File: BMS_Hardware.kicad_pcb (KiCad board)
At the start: 2 copper layers, 16.4 x 2.4 mm, 27 parts, among them Q1 2N7002PW, Q2 2N7002PW, Q3 2N7002PW, Q4 2N7002PW, Q5 2N7002PW, Q8 2N7002PW, Q9 2N7002PW, U1 ACS759ECB-200B-PFF-T, U10 E_STOP+LED, U11 TEMP_1, U12 FAN_4, U17 Indicator Comm, U18 OKI, U2 FAN_1, U21 TM4C129E_Launchpad, U4 FAN_2, U5 LOGIC_SWITCH, U6 LT1910, U7 E_STOP, U8 FAN_3

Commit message: started board edgecuts
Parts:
- added C1: 1u, Capacitor_SMD:C_0603_1608Metric_Pad1.05x0.95mm_HandSolder, F.Cu at (350.1, 110.8)
- added C10: 10u, Capacitor_SMD:C_0603_1608Metric_Pad1.05x0.95mm_HandSolder, F.Cu at (346.4, 112.8)
- added C11: 1u, Capacitor_SMD:C_0603_1608Metric_Pad1.05x0.95mm_HandSolder, F.Cu at (350.1, 107.7)
- added C12: 1u, Capacitor_SMD:C_0603_1608Metric_Pad1.05x0.95mm_HandSolder, F.Cu at (357.1, 100.9)
- added C13: 1u, Capacitor_SMD:C_0603_1608Metric_Pad1.05x0.95mm_HandSolder, F.Cu at (329.3, 130.2)
- added C14: 1u, Capacitor_SMD:C_0603_1608Metric_Pad1.05x0.95mm_HandSolder, F.Cu at (343.1, 115.9)
- added C15: 1u, Capacitor_SMD:C_0603_1608Metric_Pad1.05x0.95mm_HandSolder, F.Cu at (314.0, 114.6)
- added C16: 1u, Capacitor_SMD:C_0603_1608Metric_Pad1.05x0.95mm_HandSolder, F.Cu at (343.1, 114.4)
- added C17: 22u 50V, Capacitor_THT:CP_Radial_D6.3mm_P2.50mm, F.Cu at (350.8, 102.0)
- added C18: 10u, Capacitor_SMD:C_0603_1608Metric_Pad1.05x0.95mm_HandSolder, F.Cu at (336.0, 130.9)
- added C19: 10u, Capacitor_SMD:C_0603_1608Metric_Pad1.05x0.95mm_HandSolder, F.Cu at (353.5, 112.3)
- added C2: 1u, Capacitor_SMD:C_0603_1608Metric_Pad1.05x0.95mm_HandSolder, F.Cu at (343.1, 117.4)
- added C20: 10u, Capacitor_SMD:C_0603_1608Metric_Pad1.05x0.95mm_HandSolder, F.Cu at (343.7, 121.9)
- added C23: 10u, Capacitor_SMD:C_0603_1608Metric_Pad1.05x0.95mm_HandSolder, F.Cu at (347.0, 118.8)
- added C24: 0.1u, Capacitor_SMD:C_0603_1608Metric_Pad1.05x0.95mm_HandSolder, F.Cu at (339.6, 127.2)
- added C26: 22u 50V, Capacitor_THT:CP_Radial_D6.3mm_P2.50mm, F.Cu at (330.6, 122.2)
- added C27: 10u, Capacitor_SMD:C_0603_1608Metric_Pad1.05x0.95mm_HandSolder, F.Cu at (349.8, 116.8)
- added C28: 10u, Capacitor_SMD:C_0603_1608Metric_Pad1.05x0.95mm_HandSolder, F.Cu at (336.9, 121.1)
- added C29: 10u, Capacitor_SMD:C_0603_1608Metric_Pad1.05x0.95mm_HandSolder, F.Cu at (332.9, 126.4)
- added C3: 1u, Capacitor_SMD:C_0603_1608Metric_Pad1.05x0.95mm_HandSolder, F.Cu at (346.4, 114.3)
- added C30: 10u, Capacitor_SMD:C_0603_1608Metric_Pad1.05x0.95mm_HandSolder, F.Cu at (332.6, 129.6)
- added C31: 0.1u, Capacitor_SMD:C_0603_1608Metric_Pad1.05x0.95mm_HandSolder, F.Cu at (350.1, 112.3)
- added C4: 1u, Capacitor_SMD:C_0603_1608Metric_Pad1.05x0.95mm_HandSolder, F.Cu at (332.9, 127.9)
- added C5: 1u, Capacitor_SMD:C_0603_1608Metric_Pad1.05x0.95mm_HandSolder, F.Cu at (340.3, 119.2)
- added C6: 1u, Capacitor_SMD:C_0603_1608Metric_Pad1.05x0.95mm_HandSolder, F.Cu at (336.9, 122.7)
- added C7: 1u, Capacitor_SMD:C_0603_1608Metric_Pad1.05x0.95mm_HandSolder, F.Cu at (357.1, 102.4)
- added C8: 1u, Capacitor_SMD:C_0603_1608Metric_Pad1.05x0.95mm_HandSolder, F.Cu at (350.1, 109.3)
- added C9: 1u, Capacitor_SMD:C_0603_1608Metric_Pad1.05x0.95mm_HandSolder, F.Cu at (353.5, 106.2)
- added D1: 7.5V, Diode_SMD:D_SOD-323_HandSoldering, F.Cu at (308.0, 127.7)
- added D10: V_OUT_LED, LED_SMD:LED_0603_1608Metric_Pad1.05x0.95mm_HandSolder, F.Cu at (343.1, 112.8)
- added D11: 3.6V, Diode_SMD:D_SOD-323_HandSoldering, F.Cu at (402.5, 175.1)
- added D12: D_Schottky, Diode_SMD:D_0603_1608Metric_Pad1.05x0.95mm_HandSolder, F.Cu at (350.2, 106.2)
- added D13: D_Schottky, Diode_SMD:D_0603_1608Metric_Pad1.05x0.95mm_HandSolder, F.Cu at (357.2, 99.3)
- added D14: D_Schottky, Diode_SMD:D_0603_1608Metric_Pad1.05x0.95mm_HandSolder, F.Cu at (329.5, 126.4)
- added D15: D_Schottky, Diode_SMD:D_0603_1608Metric_Pad1.05x0.95mm_HandSolder, F.Cu at (337.0, 119.6)
- added D16: D_Schottky, Diode_SMD:D_0603_1608Metric_Pad1.05x0.95mm_HandSolder, F.Cu at (339.7, 117.6)
- added D17: D_Schottky, Diode_SMD:D_0603_1608Metric_Pad1.05x0.95mm_HandSolder, F.Cu at (339.7, 114.4)
- added D18: D_Schottky, Diode_SMD:D_0603_1608Metric_Pad1.05x0.95mm_HandSolder, F.Cu at (315.7, 129.5)
- added D19: D_Schottky, Diode_SMD:D_0603_1608Metric_Pad1.05x0.95mm_HandSolder, F.Cu at (325.9, 130.2)
- added D2: 7.5V, Diode_SMD:D_SOD-323_HandSoldering, F.Cu at (312.0, 127.7)
- added D20: D_Schottky, Diode_SMD:D_0603_1608Metric_Pad1.05x0.95mm_HandSolder, F.Cu at (319.1, 130.2)
- added D21: D_Schottky, Diode_SMD:D_0603_1608Metric_Pad1.05x0.95mm_HandSolder, F.Cu at (322.5, 130.2)
- added D22: D_Schottky, Diode_SMD:D_0603_1608Metric_Pad1.05x0.95mm_HandSolder, F.Cu at (339.7, 116.0)
- added D23: D_Schottky, Diode_SMD:D_0603_1608Metric_Pad1.05x0.95mm_HandSolder, F.Cu at (329.5, 128.0)
- added D3: 7.5V, Diode_SMD:D_SOD-323_HandSoldering, F.Cu at (316.1, 127.7)
- added D4: 7.5V, Diode_SMD:D_SOD-323_HandSoldering, F.Cu at (312.0, 129.7)
- added D5: 7.5V, Diode_SMD:D_SOD-323_HandSoldering, F.Cu at (308.0, 129.7)
- added D6: 7.5V, Diode_SMD:D_SOD-323_HandSoldering, F.Cu at (402.5, 177.0)
- added D7: 7.5V, Diode_SMD:D_SOD-323_HandSoldering, F.Cu at (314.4, 112.8)
- added D8: 7.5V, Diode_SMD:D_SOD-323_HandSoldering, F.Cu at (314.4, 110.9)
- added D9: LOG_PWR_LED, LED_SMD:LED_0603_1608Metric_Pad1.05x0.95mm_HandSolder, F.Cu at (339.7, 112.8)
- added F1: PTC2920, Fuse:Fuse_2920_7451Metric, F.Cu at (323.2, 126.4)
- added Q6: IRLS3034-7P, MRDT_Actives:IRLS3034_TO-263-7_P, F.Cu at (310.2, 121.1)
- added Q7: IRLS3034-7P, MRDT_Actives:IRLS3034_TO-263-7_P, F.Cu at (320.7, 104.2)
- added R1: 10k, Resistor_SMD:R_0603_1608Metric_Pad1.05x0.95mm_HandSolder, F.Cu at (336.9, 124.2)
- added R10: 100K, Resistor_SMD:R_0603_1608Metric_Pad1.05x0.95mm_HandSolder, F.Cu at (343.7, 120.4)
- added R11: 10K, Resistor_SMD:R_0603_1608Metric_Pad1.05x0.95mm_HandSolder, F.Cu at (340.3, 123.7)
- added R12: 100K, Resistor_SMD:R_0603_1608Metric_Pad1.05x0.95mm_HandSolder, F.Cu at (356.9, 106.9)
- added R13: 10k, Resistor_SMD:R_0603_1608Metric_Pad1.05x0.95mm_HandSolder, F.Cu at (346.4, 117.3)
- added R14: 1M, Resistor_SMD:R_0603_1608Metric_Pad1.05x0.95mm_HandSolder, F.Cu at (349.8, 113.8)
- added R15: 100k, Resistor_SMD:R_0603_1608Metric_Pad1.05x0.95mm_HandSolder, F.Cu at (353.5, 110.8)
- added R16: 10k, Resistor_SMD:R_0603_1608Metric_Pad1.05x0.95mm_HandSolder, F.Cu at (336.0, 129.4)
- added R17: 36.5k, Resistor_SMD:R_0603_1608Metric_Pad1.05x0.95mm_HandSolder, F.Cu at (349.8, 115.3)
- added R18: 4k, Resistor_SMD:R_0603_1608Metric_Pad1.05x0.95mm_HandSolder, F.Cu at (356.8, 108.4)
- added R19: 10k, Resistor_SMD:R_0603_1608Metric_Pad1.05x0.95mm_HandSolder, F.Cu at (353.5, 109.3)
- added R2: 36.5k, Resistor_SMD:R_0603_1608Metric_Pad1.05x0.95mm_HandSolder, F.Cu at (357.1, 103.9)
- added R20: 100K, Resistor_SMD:R_0603_1608Metric_Pad1.05x0.95mm_HandSolder, F.Cu at (343.6, 123.5)
- added R21: 36.5k, Resistor_SMD:R_0603_1608Metric_Pad1.05x0.95mm_HandSolder, F.Cu at (353.1, 113.8)
- added R22: 1M, Resistor_SMD:R_0603_1608Metric_Pad1.05x0.95mm_HandSolder, F.Cu at (356.8, 110.0)
- added R23: 100k, Resistor_SMD:R_0603_1608Metric_Pad1.05x0.95mm_HandSolder, F.Cu at (340.3, 125.2)
- added R24: 100K, Resistor_SMD:R_0603_1608Metric_Pad1.05x0.95mm_HandSolder, F.Cu at (339.3, 128.7)
- added R25: 330, Resistor_SMD:R_0603_1608Metric_Pad1.05x0.95mm_HandSolder, F.Cu at (356.8, 111.5)
- added R26: 330, Resistor_SMD:R_0603_1608Metric_Pad1.05x0.95mm_HandSolder, F.Cu at (353.1, 115.3)
- added R27: 1M, Resistor_SMD:R_0603_1608Metric_Pad1.05x0.95mm_HandSolder, F.Cu at (343.6, 125.0)
- added R28: 100k, Resistor_SMD:R_0603_1608Metric_Pad1.05x0.95mm_HandSolder, F.Cu at (347.0, 121.9)
- added R29: 4.7k, Resistor_SMD:R_0603_1608Metric_Pad1.05x0.95mm_HandSolder, F.Cu at (350.4, 118.3)
- added R3: 10k, Resistor_SMD:R_0603_1608Metric_Pad1.05x0.95mm_HandSolder, F.Cu at (353.5, 107.7)
- added R30: 36.5k, Resistor_SMD:R_0603_1608Metric_Pad1.05x0.95mm_HandSolder, F.Cu at (342.9, 126.7)
- added R31: 36.5k, Resistor_SMD:R_0603_1608Metric_Pad1.05x0.95mm_HandSolder, F.Cu at (340.3, 120.7)
- added R32: 36.5k, Resistor_SMD:R_0603_1608Metric_Pad1.05x0.95mm_HandSolder, F.Cu at (353.1, 116.8)
- added R33: 36.5k, Resistor_SMD:R_0603_1608Metric_Pad1.05x0.95mm_HandSolder, F.Cu at (356.8, 113.0)
- added R34: 36.5k, Resistor_SMD:R_0603_1608Metric_Pad1.05x0.95mm_HandSolder, F.Cu at (336.2, 127.2)
- added R4: 10k, Resistor_SMD:R_0603_1608Metric_Pad1.05x0.95mm_HandSolder, F.Cu at (357.1, 105.4)
- added R5: 10k, Resistor_SMD:R_0603_1608Metric_Pad1.05x0.95mm_HandSolder, F.Cu at (336.9, 125.7)
- added R6: 10k, Resistor_SMD:R_0603_1608Metric_Pad1.05x0.95mm_HandSolder, F.Cu at (340.3, 122.2)
- added R7: 10k, Resistor_SMD:R_0603_1608Metric_Pad1.05x0.95mm_HandSolder, F.Cu at (347.0, 120.4)
- added R8: 10k, Resistor_SMD:R_0603_1608Metric_Pad1.05x0.95mm_HandSolder, F.Cu at (343.7, 118.9)
- added R9: 10k, Resistor_SMD:R_0603_1608Metric_Pad1.05x0.95mm_HandSolder, F.Cu at (346.4, 115.8)
- added U13: INA132, Package_SO:SO-8_5.3x6.2mm_P1.27mm, F.Cu at (333.9, 108.7)
- added U14: INA132, Package_SO:SO-8_5.3x6.2mm_P1.27mm, F.Cu at (391.3, 63.9)
- added U15: INA132, Package_SO:SO-8_5.3x6.2mm_P1.27mm, F.Cu at (323.4, 120.0)
- added U16: OKI, MRDT_Devices:OKI_Horizontal, F.Cu at (302.1, 98.8)
- added U19: INA132, Package_SO:SO-8_5.3x6.2mm_P1.27mm, F.Cu at (333.1, 115.4)
- added U20: INA132, Package_SO:SO-8_5.3x6.2mm_P1.27mm, F.Cu at (343.6, 108.7)
- added U3: INA132, Package_SO:SO-8_5.3x6.2mm_P1.27mm, F.Cu at (333.9, 101.9)
- added U9: INA132, Package_SO:SO-8_5.3x6.2mm_P1.27mm, F.Cu at (323.4, 113.3)
- moved Q5 209.7 mm to (310.4, 177.4)
- moved Conn2 209.7 mm to (340.8, 171.7)
- moved Q4 209.7 mm to (315.9, 177.4)
- moved U11 209.7 mm to (341.1, 176.0)
- moved U12 209.7 mm to (373.3, 171.5)
- moved U17 209.7 mm to (351.6, 176.0)
- moved U2 209.7 mm to (373.3, 178.0)
- moved U5 209.7 mm to (360.0, 171.7)
- moved U7 209.7 mm to (381.0, 171.5)
- moved U8 209.7 mm to (381.0, 178.0)
- moved C32 209.7 mm to (317.6, 171.5)
- moved Q3 209.7 mm to (321.3, 177.4)
- moved Q8 209.7 mm to (305.0, 177.4)
- moved Q9 209.7 mm to (299.5, 177.4)
- moved U10 209.7 mm to (334.4, 178.5)
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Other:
- board size 16.4 x 2.4 mm -> 208.3 x 76.2 mm

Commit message: work done on board layout
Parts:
- moved U8 348.4 mm to (48.0, 75.7)
- moved U2 346.4 mm to (48.0, 59.1)
- moved U12 336.9 mm to (48.0, 83.9)
- moved U4 336.5 mm to (48.0, 67.3)
- moved U7 336.1 mm to (64.6, 58.1)
- moved U5 307.8 mm to (66.8, 77.8)
- moved V1 307.5 mm to (61.7, 105.8)
- moved R12 305.0 mm to (54.9, 64.7)
- moved Q1 301.3 mm to (54.8, 59.7), turned to 270 degrees
- moved R10 296.1 mm to (54.8, 55.7)
- moved R20 292.9 mm to (55.0, 73.6)
- moved R18 289.5 mm to (71.4, 60.4)
- moved U10 289.3 mm to (67.0, 68.1)
- moved R24 288.1 mm to (55.0, 82.2)
- moved R19 283.0 mm to (75.5, 55.9)
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
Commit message: halfway done with alyout
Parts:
- moved C19 180.6 mm to (183.4, 104.3), turned to 90 degrees
- moved C17 179.5 mm to (171.8, 114.4), turned to 90 degrees
- moved C27 172.2 mm to (179.9, 88.4), turned to 270 degrees
- moved C26 160.5 mm to (171.9, 98.1), turned to 90 degrees
- moved C18 159.0 mm to (179.2, 104.2), turned to 90 degrees
- moved C20 157.1 mm to (187.6, 104.2), turned to 90 degrees
- moved C28 156.4 mm to (184.0, 88.4), turned to 270 degrees
- moved C23 156.0 mm to (191.7, 104.2), turned to 90 degrees
- moved C31 155.7 mm to (196.2, 88.5), turned to 270 degrees
- moved C29 149.7 mm to (188.1, 88.5), turned to 270 degrees
- moved C30 146.4 mm to (192.1, 88.5), turned to 270 degrees
- moved C24 145.6 mm to (195.8, 104.2), turned to 90 degrees
- moved U18 142.9 mm to (179.1, 100.8), turned to 90 degrees
- moved U16 131.6 mm to (179.2, 116.9), turned to 90 degrees
- moved Conn1 15.5 mm to (152.0, 64.3)
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
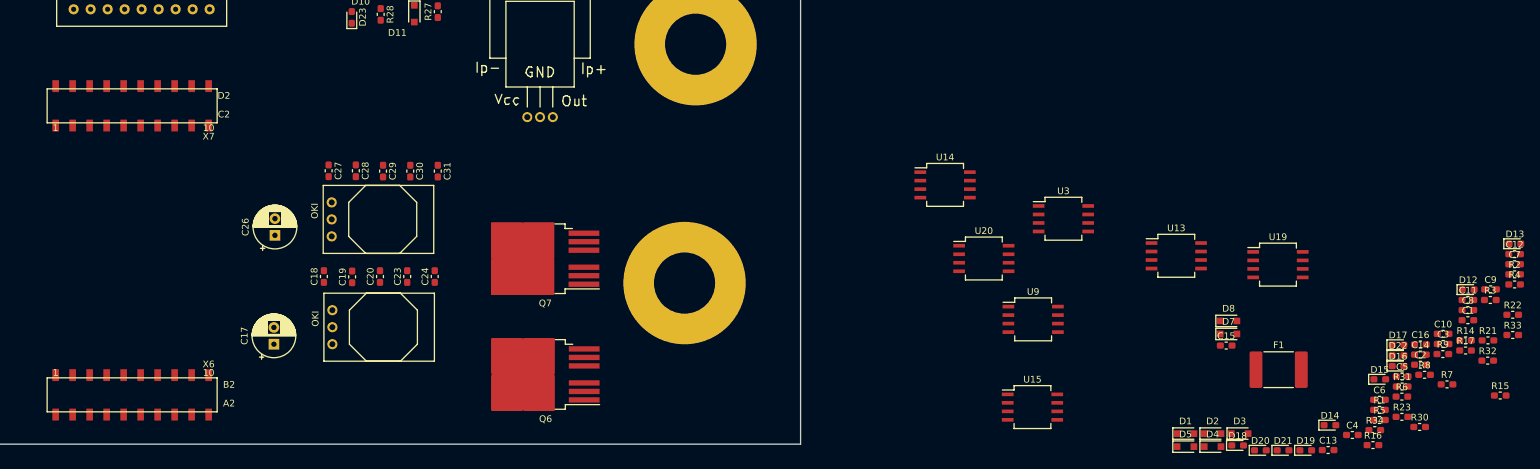
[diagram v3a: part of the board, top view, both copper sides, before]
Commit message: added half of the diffamp circuits
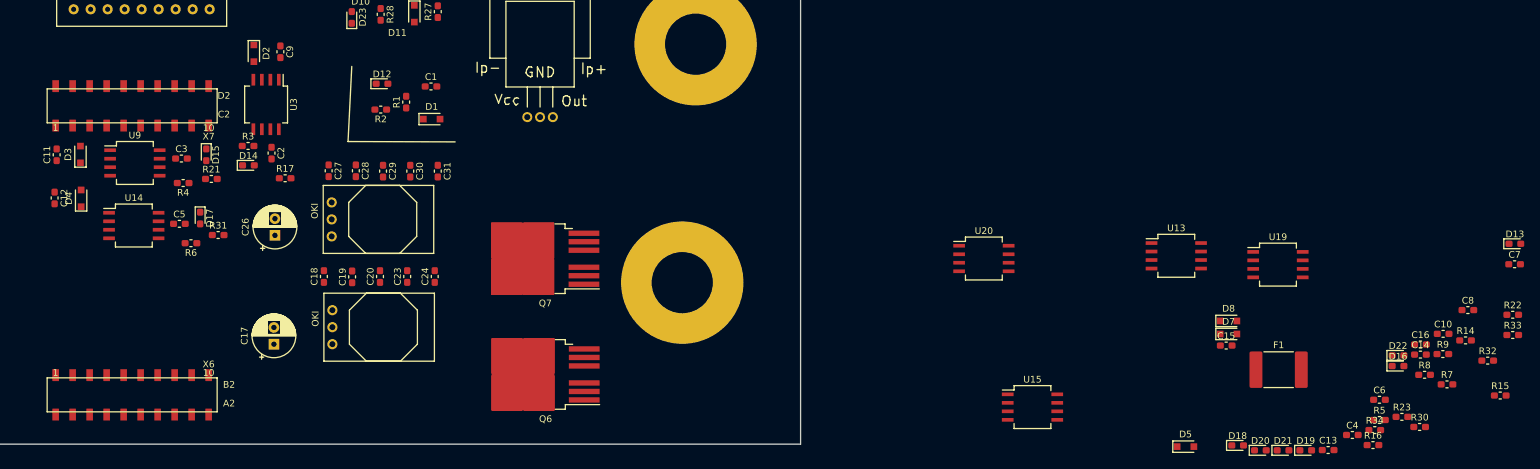
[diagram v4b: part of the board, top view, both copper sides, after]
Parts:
- moved C12 218.3 mm to (139.0, 92.5), turned to 270 degrees
- moved C11 212.0 mm to (139.3, 86.1), turned to 90 degrees
- moved R4 199.5 mm to (158.2, 90.3), turned to 180 degrees
- moved R21 192.3 mm to (162.4, 89.7)
- moved C3 190.5 mm to (157.9, 86.6)
- moved R3 187.0 mm to (167.9, 84.7)
- moved C9 184.3 mm to (172.7, 70.7), turned to 270 degrees
- moved C5 184.1 mm to (157.6, 96.4)
- moved R6 182.4 mm to (159.4, 99.3), turned to 180 degrees
- moved D17 180.0 mm to (160.7, 95.5), turned to 270 degrees
- moved D15 178.5 mm to (161.6, 86.1), turned to 270 degrees
- moved R31 178.3 mm to (163.4, 98.0)
- moved R17 178.2 mm to (173.4, 89.6)
- moved D3 178.2 mm to (142.8, 86.0), turned to 90 degrees
- moved C2 174.5 mm to (171.4, 85.8), turned to 270 degrees
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
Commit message: finished board layout
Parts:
- moved R9 281.1 mm to (69.7, 66.5), turned to 90 degrees
- moved C10 251.9 mm to (95.7, 88.8)
- moved R15 250.3 mm to (108.6, 77.8), turned to 180 degrees
- moved D13 244.3 mm to (113.9, 76.7), turned to 180 degrees
- moved D21 240.8 mm to (86.0, 84.7), turned to 180 degrees
- moved R14 240.7 mm to (112.8, 71.4), turned to 270 degrees
- moved C16 237.4 mm to (107.2, 87.8), turned to 90 degrees
- moved C7 232.9 mm to (124.3, 94.8)
- moved U6 229.9 mm to (89.0, 89.8)
- moved C8 227.0 mm to (124.4, 85.5)
- moved R33 225.3 mm to (132.1, 97.4)
- moved R7 222.6 mm to (124.4, 116.9), turned to 270 degrees
- moved R32 222.1 mm to (131.1, 112.9)
- moved F1 220.7 mm to (106.1, 71.5), turned to 180 degrees
- moved R8 220.2 mm to (124.4, 99.0), turned to 180 degrees
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
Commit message: layout revisions
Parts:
- moved C32 112.3 mm to (214.9, 116.8), turned to 270 degrees
- moved C23 111.9 mm to (278.5, 33.8)
- moved C24 111.9 mm to (282.7, 33.8)
- moved C19 111.9 mm to (270.3, 33.8)
- moved C17 111.9 mm to (258.6, 43.9)
- moved C18 111.9 mm to (266.1, 33.8)
- moved C20 111.9 mm to (274.5, 33.8)
- moved U16 111.9 mm to (266.1, 46.4)
- moved R22 88.4 mm to (123.3, 56.1)
- moved R23 88.4 mm to (118.7, 56.2)
- moved D22 88.4 mm to (113.4, 56.3)
- moved C2 55.9 mm to (118.8, 75.3)
- moved D14 55.9 mm to (116.9, 71.9)
- moved R3 55.9 mm to (119.8, 71.8)
- moved U3 55.9 mm to (126.0, 74.5)
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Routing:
- added copper zone on F.Cu, net V_IN
- added copper zone on B.Cu, net V_OUT

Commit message: further revisions
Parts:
- U1: footprint PFF_PSF_PSS_Leadforms:PFF_Leadform_5pins -> BMS_Hardware:PFF_Leadform_5pins
- moved C32 58.3 mm to (268.7, 94.5)
- moved C27 37.9 mm to (176.3, 70.9)
- moved C28 37.9 mm to (176.3, 75.0)
- moved C29 37.9 mm to (176.3, 79.0)
- moved C30 37.9 mm to (176.3, 83.1)
- moved C31 37.9 mm to (176.3, 87.2)
- moved Q7 7.21 mm to (205.1, 96.6)
- moved Q6 7.21 mm to (205.1, 113.4)
- moved C26 4.79 mm to (170.2, 97.4)
- moved U18 4.79 mm to (167.6, 104.6)
- moved U1 3.15 mm to (204.7, 69.2), turned to 0 degrees

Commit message: revisionssss
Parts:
- moved C32 83.1 mm to (186.4, 83.3)
- moved D22 18.3 mm to (95.1, 56.8)
- moved R22 18.3 mm to (105.0, 56.7)
- moved R23 18.3 mm to (100.4, 56.7)
- moved U17 15.1 mm to (112.3, 55.9)
- moved Conn1 9.65 mm to (142.3, 64.3)
- moved Conn2 9.65 mm to (142.3, 57.6)
- moved D10 9.14 mm to (163.2, 59.7)
- moved D11 9.14 mm to (171.3, 62.9)
- moved D9 9.14 mm to (162.9, 55.3)
- moved R25 9.14 mm to (168.6, 55.3)
- moved R26 9.14 mm to (168.8, 59.7)
- moved R27 9.14 mm to (174.8, 62.6)
- moved R28 9.14 mm to (166.2, 63.0)
- moved D23 9.14 mm to (161.9, 63.5)
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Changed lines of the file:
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@@
   )
   (module MRDT_Connectors:Anderson_2_Vertical (layer F.Cu)
-    (at 268.732 94.488 270)
+    (at 186.436 83.312 270)
     (fp_text reference C32 (at -6.1722 3.1496 270) (layer F.Fab) hide
       (effects (font (size 1 1) (thickness 0.15)))
@@
   )
   (module MRDT_Connectors:MOLEX_SL_09_Vertical (layer F.Cu)
-    (at 151.9936 64.3128)
+    (at 142.3416 64.3128)
     (fp_text reference Conn1 (at -10.795 3.683) (layer F.SilkS) hide
       (effects (font (size 1 1) (thickness 0.15)))
@@
   )
   (module MRDT_Connectors:MOLEX_SL_09_Vertical (layer F.Cu)
-    (at 151.9936 57.6072)
+    (at 142.3416 57.6072)
     (fp_text reference Conn2 (at -8.1788 -5.7912) (layer F.SilkS) hide
       (effects (font (size 1 1) (thickness 0.15)))
@@
   )
   (module TO_SOT_Packages_SMD:SOT-23_Handsoldering (layer F.Cu)
-    (at 182.9054 56.8452 270)
+    (at 173.7614 56.8452 270)
     (descr "SOT-23, Handsoldering")
     (tags SOT-23)
@@
   )
   (module MRDT_Connectors:MOLEX_SL_03_Vertical (layer F.Cu)
-    (at 127.381 55.245)
+    (at 112.268 55.88)
     (fp_text reference U17 (at 1.524 4.3561) (layer F.SilkS) hide
       (effects (font (size 1 1) (thickness 0.15)))
@@
   )
   (module LED_SMD:LED_0603_1608Metric_Pad1.05x0.95mm_HandSolder (layer F.Cu)
-    (at 172.085 55.3212 180)
+    (at 162.941 55.3212 180)
     (descr "LED SMD 0603 (1608 Metric), square (rectangular) end terminal, IPC_7351 nominal, (Body size source: http://www.tortai-tech.com/upload/download/2011102023233369053.pdf), generated with kicad-footprint-generator")
     (tags "LED handsolder")
@@
   )
   (module LED_SMD:LED_0603_1608Metric_Pad1.05x0.95mm_HandSolder (layer F.Cu)
-    (at 172.3898 59.69 180)
+    (at 163.2458 59.69 180)
     (descr "LED SMD 0603 (1608 Metric), square (rectangular) end terminal, IPC_7351 nominal, (Body size source: http://www.tortai-tech.com/upload/download/2011102023233369053.pdf), generated with kicad-footprint-generator")
     (tags "LED handsolder")
@@
   )
   (module Diode_SMD:D_SOD-323_HandSoldering (layer F.Cu)
-    (at 180.4162 62.9412 270)
+    (at 171.2722 62.9412 270)
     (descr SOD-323)
     (tags SOD-323)
@@
   )
   (module Diode_SMD:D_0603_1608Metric_Pad1.05x0.95mm_HandSolder (layer F.Cu)
-    (at 113.4377 56.3372)
+    (at 95.1497 56.8452)
     (descr "Diode SMD 0603 (1608 Metric), square (rectangular) end terminal, IPC_7351 nominal, (Body size source: http://www.tortai-tech.com/upload/download/2011102023233369053.pdf), generated with kicad-footprint-generator")
     (tags "diode handsolder")
@@
   )
   (module Diode_SMD:D_0603_1608Metric_Pad1.05x0.95mm_HandSolder (layer F.Cu)
-    (at 171.069 63.5 90)
+    (at 161.925 63.5 90)
     (descr "Diode SMD 0603 (1608 Metric), square (rectangular) end terminal, IPC_7351 nominal, (Body size source: http://www.tortai-tech.com/upload/download/2011102023233369053.pdf), generated with kicad-footprint-generator")
     (tags "diode handsolder")
@@
   )
   (module Resistor_SMD:R_0603_1608Metric_Pad1.05x0.95mm_HandSolder (layer F.Cu)
-    (at 123.2916 56.1467 180)
+    (at 105.0036 56.6547 180)
     (descr "Resistor SMD 0603 (1608 Metric), square (rectangular) end terminal, IPC_7351 nominal with elongated pad for handsoldering. (Body size source: http://www.tortai-tech.com/upload/download/2011102023233369053.pdf), generated with kicad-footprint-generator")
     (tags "resistor handsolder")
@@
   )
   (module Resistor_SMD:R_0603_1608Metric_Pad1.05x0.95mm_HandSolder (layer F.Cu)
-    (at 118.6828 56.2229)
+    (at 100.3948 56.7309)
     (descr "Resistor SMD 0603 (1608 Metric), square (rectangular) end terminal, IPC_7351 nominal with elongated pad for handsoldering. (Body size source: http://www.tortai-tech.com/upload/download/2011102023233369053.pdf), generated with kicad-footprint-generator")
     (tags "resistor handsolder")
@@
   )
   (module Resistor_SMD:R_0603_1608Metric_Pad1.05x0.95mm_HandSolder (layer F.Cu)
-    (at 177.7238 55.3212)
+    (at 168.5798 55.3212)
     (descr "Resistor SMD 0603 (1608 Metric), square (rectangular) end terminal, IPC_7351 nominal with elongated pad for handsoldering. (Body size source: http://www.tortai-tech.com/upload/download/2011102023233369053.pdf), generated with kicad-footprint-generator")
     (tags "resistor handsolder")
@@
   )
   (module Resistor_SMD:R_0603_1608Metric_Pad1.05x0.95mm_HandSolder (layer F.Cu)
-    (at 177.927 59.69)
+    (at 168.783 59.69)
     (descr "Resistor SMD 0603 (1608 Metric), square (rectangular) end terminal, IPC_7351 nominal with elongated pad for handsoldering. (Body size source: http://www.tortai-tech.com/upload/download/2011102023233369053.pdf), generated with kicad-footprint-generator")
     (tags "resistor handsolder")
@@
   )
   (module Resistor_SMD:R_0603_1608Metric_Pad1.05x0.95mm_HandSolder (layer F.Cu)
-    (at 183.9214 62.6364 90)
+    (at 174.7774 62.6364 90)
     (descr "Resistor SMD 0603 (1608 Metric), square (rectangular) end terminal, IPC_7351 nominal with elongated pad for handsoldering. (Body size source: http://www.tortai-tech.com/upload/download/2011102023233369053.pdf), generated with kicad-footprint-generator")
     (tags "resistor handsolder")
@@
   )
   (module Resistor_SMD:R_0603_1608Metric_Pad1.05x0.95mm_HandSolder (layer F.Cu)
-    (at 175.387 63.0428 270)
+    (at 166.243 63.0428 270)
     (descr "Resistor SMD 0603 (1608 Metric), square (rectangular) end terminal, IPC_7351 nominal with elongated pad for handsoldering. (Body size source: http://www.tortai-tech.com/upload/download/2011102023233369053.pdf), generated with kicad-footprint-generator")
     (tags "resistor handsolder")
